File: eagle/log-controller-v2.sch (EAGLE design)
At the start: 23 parts, among them Q1 IRLB8721PBFTO220AB, T1 2N3055, T2 BC547, X1 Power/Motor

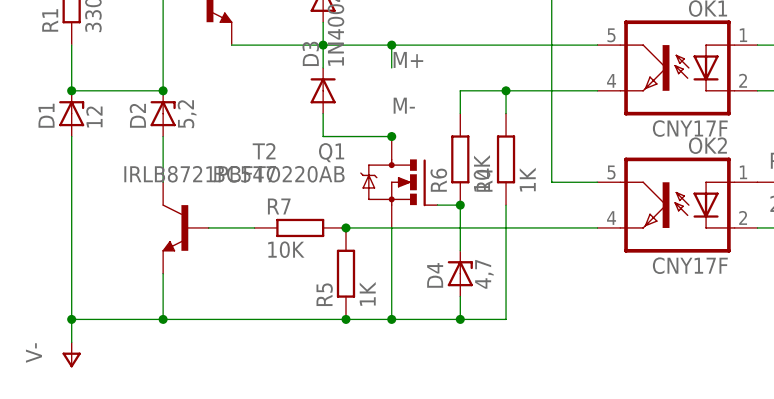
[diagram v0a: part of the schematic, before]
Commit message: Changed a resistor due to the electronic gearbox not working.
Seems not to have solved it completely... back to the drawing board.
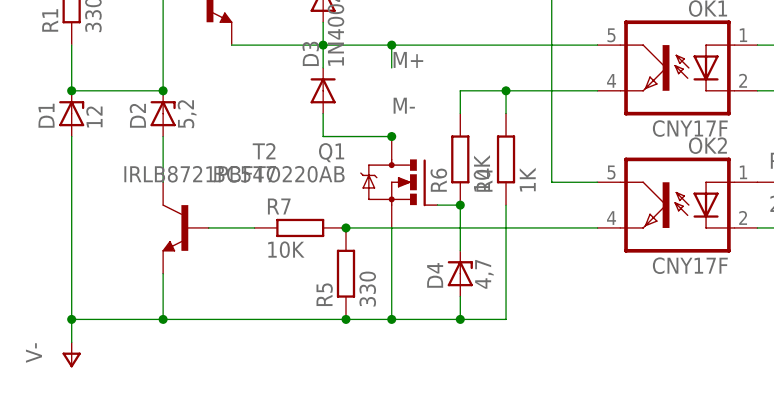
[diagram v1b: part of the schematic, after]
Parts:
- R5: value 1K -> 330
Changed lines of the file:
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@@
 <part name="P-1" library="supply1" deviceset="V-" device=""/>
 <part name="OK2" library="optocoupler" deviceset="CNY17F" device=""/>
-<part name="R5" library="resistor" deviceset="R-EU_" device="0207/12" value="1K"/>
+<part name="R5" library="resistor" deviceset="R-EU_" device="0207/12" value="330"/>
 <part name="R6" library="resistor" deviceset="R-EU_" device="0207/12" value="10K"/>
 <part name="R7" library="resistor" deviceset="R-EU_" device="0207/12" value="10K"/>
